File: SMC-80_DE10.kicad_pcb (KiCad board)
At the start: 4 copper layers, 63.5 x 58.4 mm, 26 parts, among them J1 Arduino1, J2 DE10-Lite GPIO, J3 Arduino2, J4 Port A, U1 SST39SF040, U2 Z84C0010AEG, U3 AS6C4008A-55ZIN, U4 Z84C4310AEG

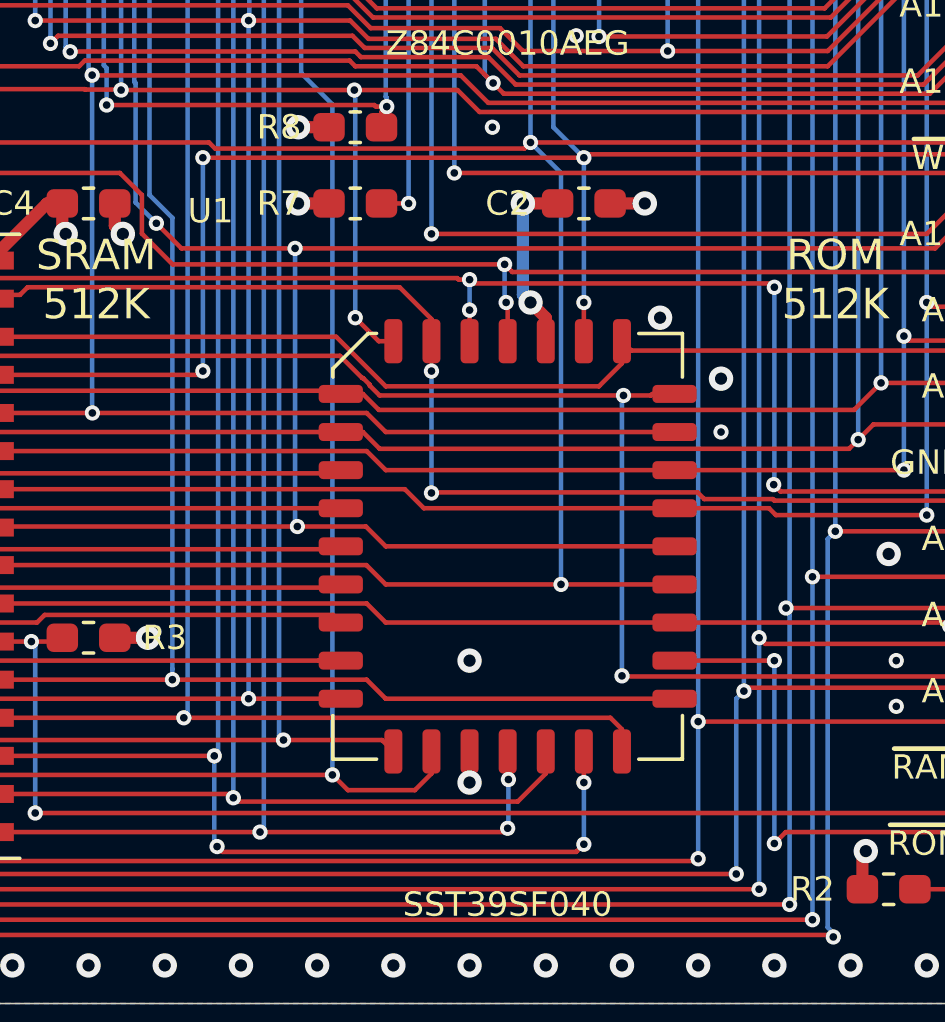
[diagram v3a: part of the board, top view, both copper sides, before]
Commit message: enhanced graphic for PLCC socket
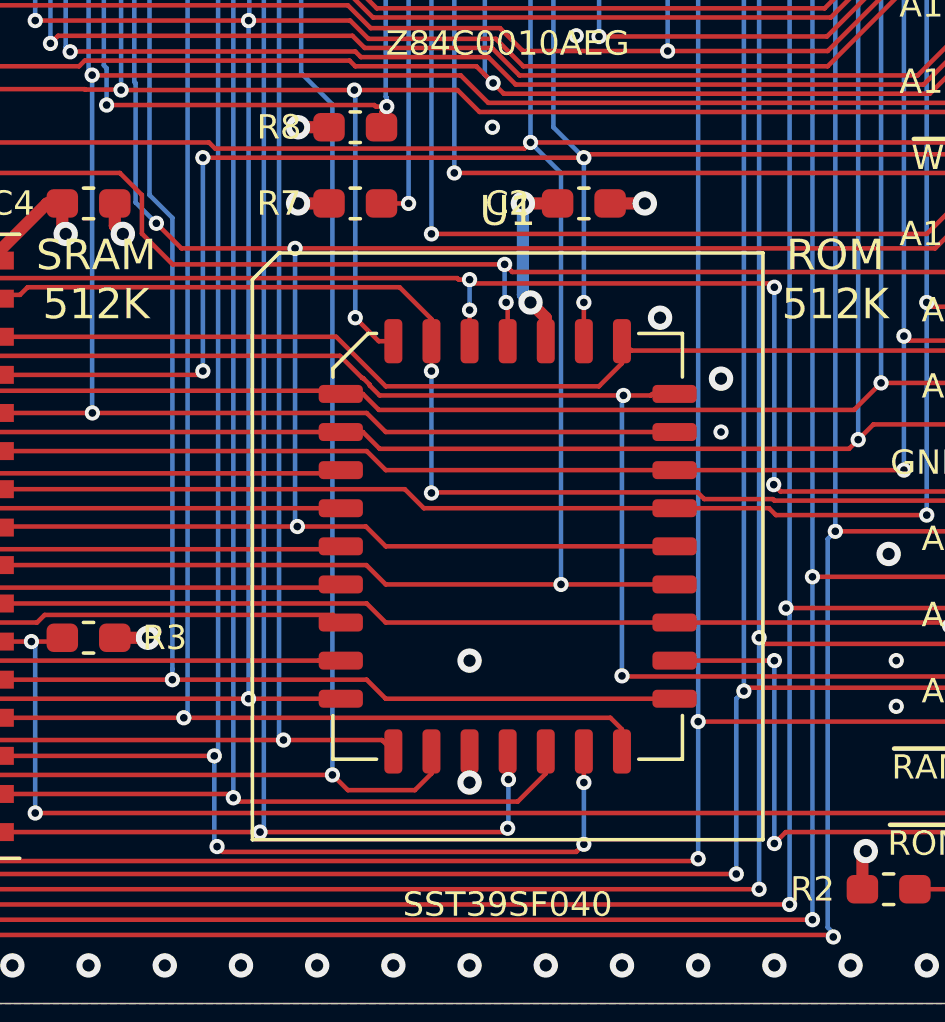
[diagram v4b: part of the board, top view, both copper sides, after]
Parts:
- U1: value SST39SF040 -> SST39LF040
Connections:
- J1 pad 1: (no net) -> Net-(J1-Pad1)
- J1 pad 2: (no net) -> Net-(J1-Pad2)
- J2 pad 1: (no net) -> Net-(J2-Pad1)
- J2 pad 11: (no net) -> +5V
- J2 pad 3: (no net) -> Net-(J2-Pad3)
- J2 pad 35: (no net) -> Net-(J2-Pad35)
- J2 pad 37: (no net) -> Net-(J2-Pad37)
- J3 pad 4: (no net) -> Net-(J3-Pad4)
- J3 pad 5: (no net) -> Net-(J3-Pad5)
- J3 pad 6: (no net) -> Net-(J3-Pad6)
- J3 pad 7: (no net) -> Net-(J3-Pad7)
- J3 pad 8: (no net) -> Net-(J3-Pad8)
- J4 pad 3: (no net) -> Net-(J4-Pad3)
- R2 pad 1: VCC -> Net-(R2-Pad1)
- U2 pad 11: (no net) -> Net-(U2-Pad11)
- U2 pad 17: (no net) -> Net-(U2-Pad17)
- U2 pad 20: (no net) -> Net-(U2-Pad20)
- U2 pad 25: (no net) -> Net-(U2-Pad25)
- U2 pad 33: (no net) -> Net-(U2-Pad33)
- U2 pad 39: (no net) -> Net-(U2-Pad39)
- U4 pad 1: (no net) -> Net-(U4-Pad1)
- U4 pad 10: (no net) -> Net-(U4-Pad10)
- U4 pad 11: (no net) -> Net-(U4-Pad11)
- U4 pad 12: (no net) -> Net-(U4-Pad12)
- U4 pad 13: (no net) -> Net-(U4-Pad13)
- U4 pad 14: (no net) -> Net-(U4-Pad14)
- U4 pad 15: (no net) -> Net-(U4-Pad15)
- U4 pad 16: (no net) -> Net-(U4-Pad16)
- U4 pad 17: (no net) -> Net-(U4-Pad17)
- U4 pad 28: (no net) -> Net-(U4-Pad28)
- U4 pad 35: (no net) -> Net-(U4-Pad35)
- U4 pad 38: (no net) -> Net-(U4-Pad38)
- U4 pad 39: (no net) -> Net-(U4-Pad39)
- U4 pad 40: (no net) -> Net-(U4-Pad40)
- U4 pad 8: (no net) -> Net-(U4-Pad8)
- U4 pad 9: (no net) -> Net-(U4-Pad9)
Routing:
- net Net-(R2-Pad1): track 0.00 -> 1.32 mm, vias 0 -> 1
- net VCC: track 32.2 -> 30.9 mm, vias 15 -> 14

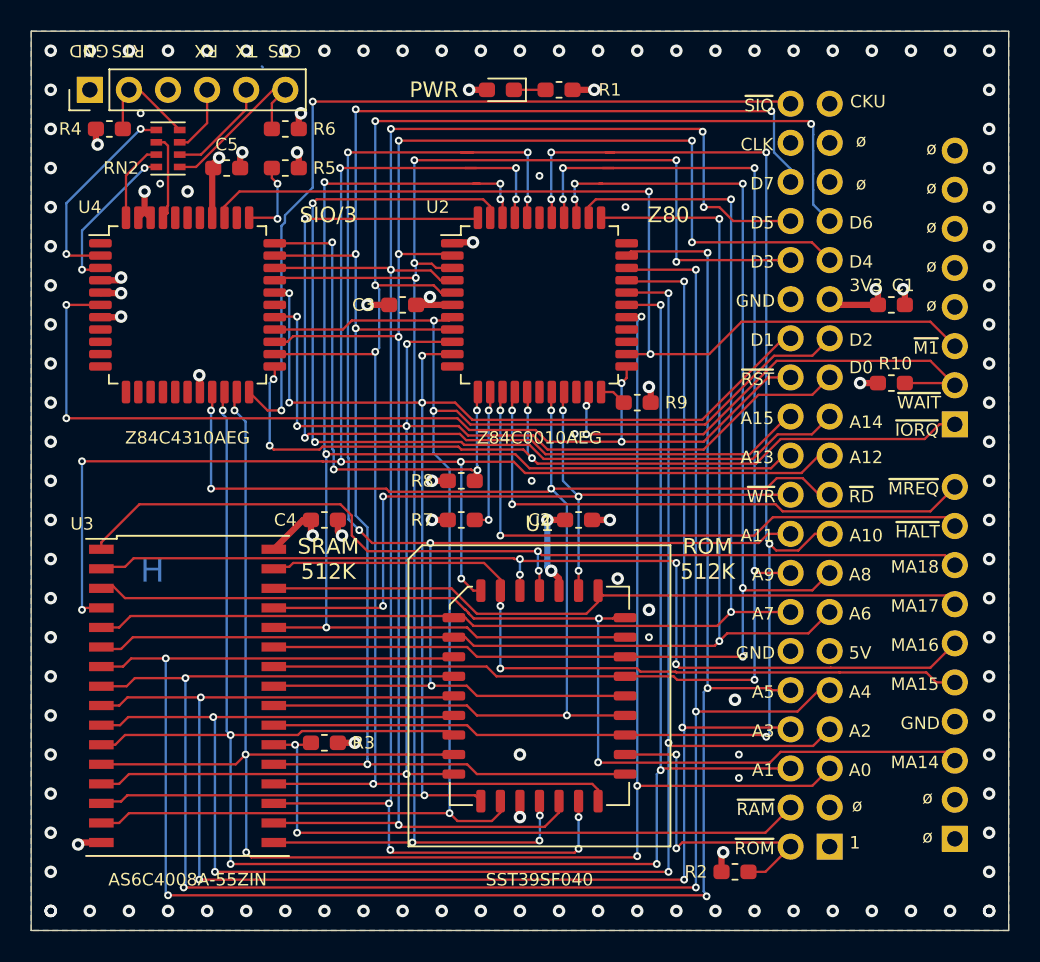
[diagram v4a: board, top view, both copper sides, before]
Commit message: removed ram/rom ce pullups
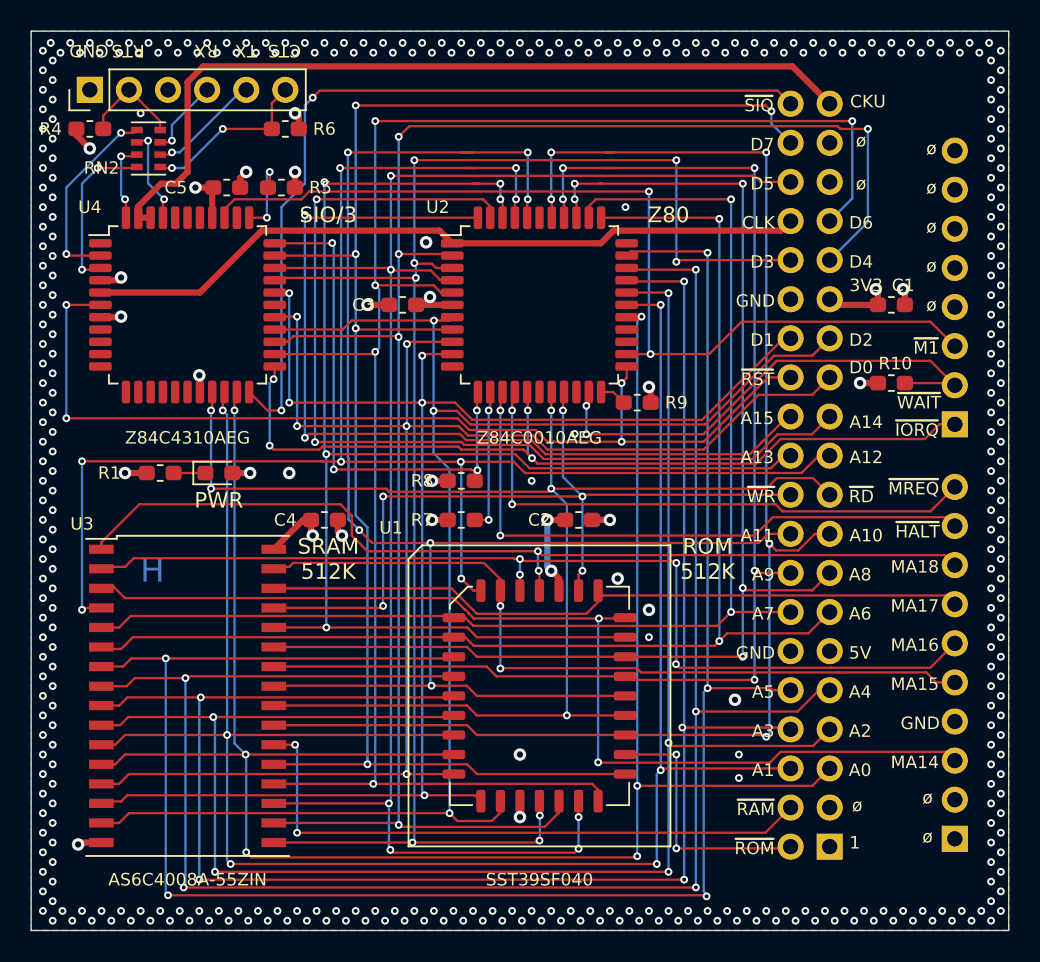
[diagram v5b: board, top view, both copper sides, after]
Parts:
- removed R2, R3: 10K, Resistor_SMD:R_0603_1608Metric_Pad1.05x0.95mm_HandSolder
- moved R1 35.9 mm to (108.7, 98.6), turned to 180 degrees
- moved D1 30.9 mm to (112.5, 98.6), turned to 0 degrees
- moved R5 1.30 mm to (116.6, 80.0)
- moved C5 1.27 mm to (113.0, 80.0)
- moved R4 1.27 mm to (104.1, 76.2)
- moved RN2 1.27 mm to (108.0, 77.5)
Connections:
- J2 pad 34: /D5 -> /CLK
- J2 pad 36: /D7 -> /D5
- J2 pad 38: /CLK -> /D7
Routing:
- net /D5: track 113.1 -> 104.9 mm, vias 8 -> 6
- net /D4: track 111.0 -> 116.6 mm, vias 6 -> 5
- net /CLK_U: track 49.9 -> 54.6 mm, vias 1 -> 0
- net /ROM_~CE: track 20.5 -> 16.9 mm
- net /CLK: track 50.9 -> 47.6 mm, vias 2 -> 0
- net /D6: track 112.3 -> 115.2 mm
- net /D7: track 109.7 -> 107.5 mm
- net VCC: track 30.9 -> 29.4 mm, vias 14 -> 13
- net Net-(R2-Pad1): track 1.32 -> 0.00 mm, vias 1 -> 0
- net Net-(J4-Pad4): track 4.46 -> 5.59 mm, vias 0 -> 1
- net /RAM_~CE: track 41.0 -> 39.9 mm
- net Net-(J4-Pad2): track 7.08 -> 7.93 mm
- net /SIO_~CE: track 54.8 -> 55.5 mm
- net /Ram Rom and CPU/~RTS: track 13.4 -> 12.8 mm
- net /Ram Rom and CPU/RX: track 5.66 -> 6.25 mm, vias 0 -> 2
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
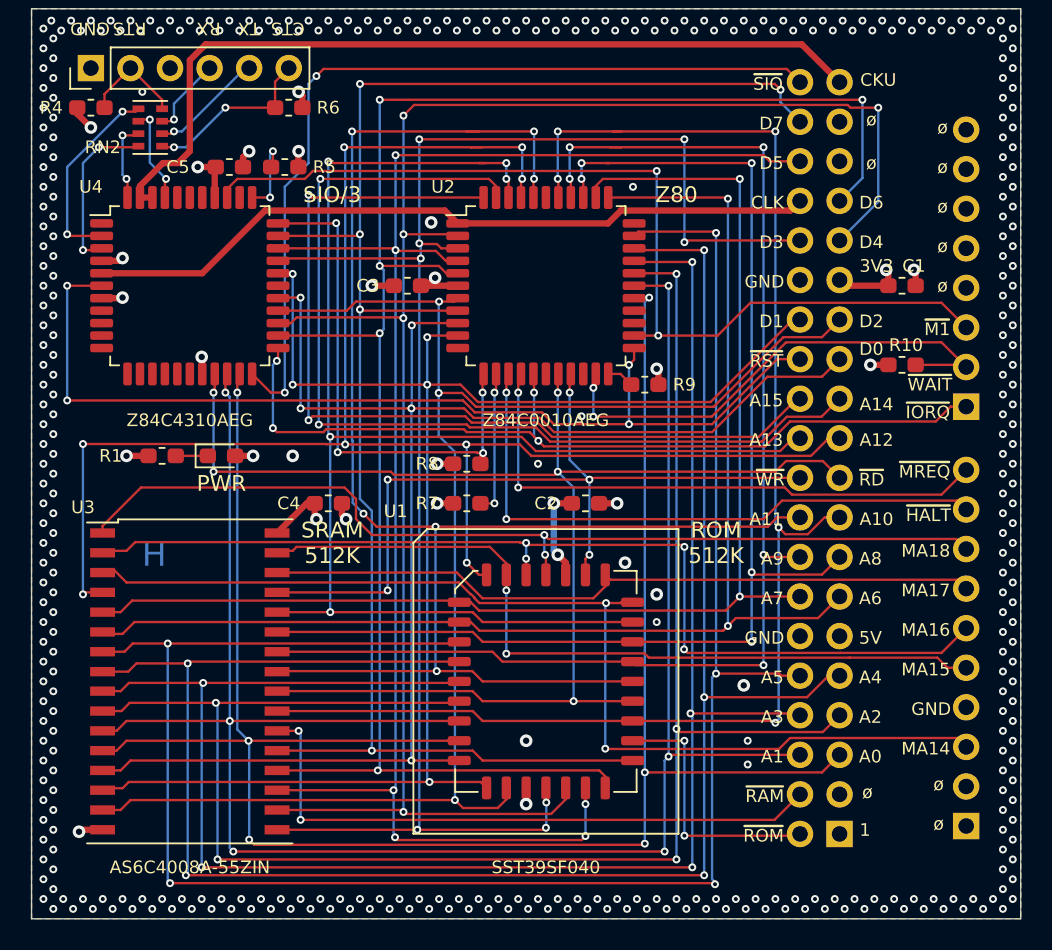
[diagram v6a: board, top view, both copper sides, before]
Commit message: shifted Arduino pins
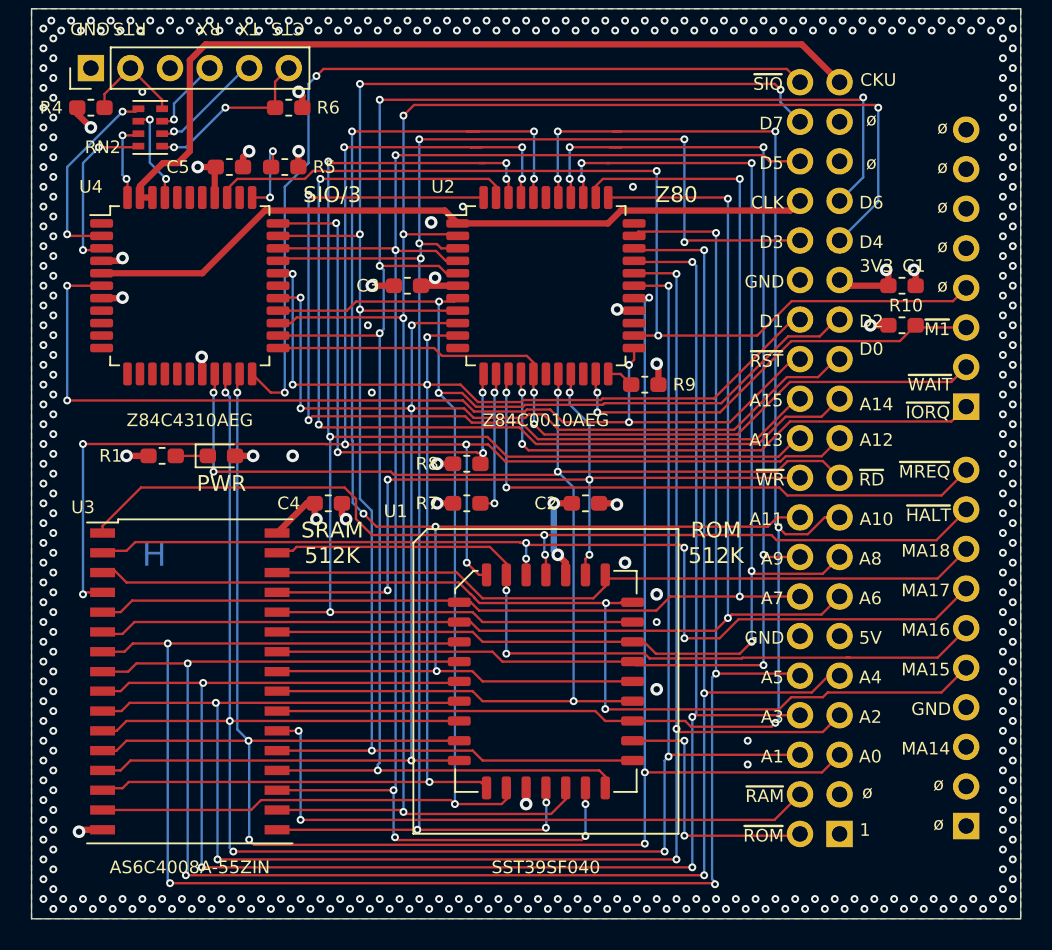
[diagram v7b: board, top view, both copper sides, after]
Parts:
- moved R10 2.54 mm to (156.2, 90.2)
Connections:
- J1 pad 10: /~MREQ -> /~HALT
- J1 pad 3: /MA14 -> Net-(J1-Pad3)
- J1 pad 5: /MA15 -> /MA14
- J1 pad 6: /MA16 -> /MA15
- J1 pad 7: /MA17 -> /MA16
- J1 pad 8: /MA18 -> /MA17
- J1 pad 9: /~HALT -> /MA18
- J3 pad 1: /~IORQ -> /~MREQ
- J3 pad 2: /~WAIT -> /~IORQ
- J3 pad 3: /~M1 -> /~WAIT
- J3 pad 4: Net-(J3-Pad4) -> /~M1
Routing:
- net /~IORQ: track 55.9 -> 50.6 mm, vias 4 -> 2
- net /~WAIT: track 32.7 -> 28.6 mm
- net /~MREQ: track 37.0 -> 34.6 mm
- net /MA14: track 68.1 -> 66.1 mm
- net /~HALT: track 39.6 -> 37.8 mm
- net GND: track 15.0 -> 16.2 mm, vias 397 -> 398
- net /MA15: track 51.0 -> 51.8 mm
- net /A8: track 81.0 -> 81.6 mm
- net /MA17: track 46.3 -> 46.9 mm
- net /A6: track 84.0 -> 83.5 mm

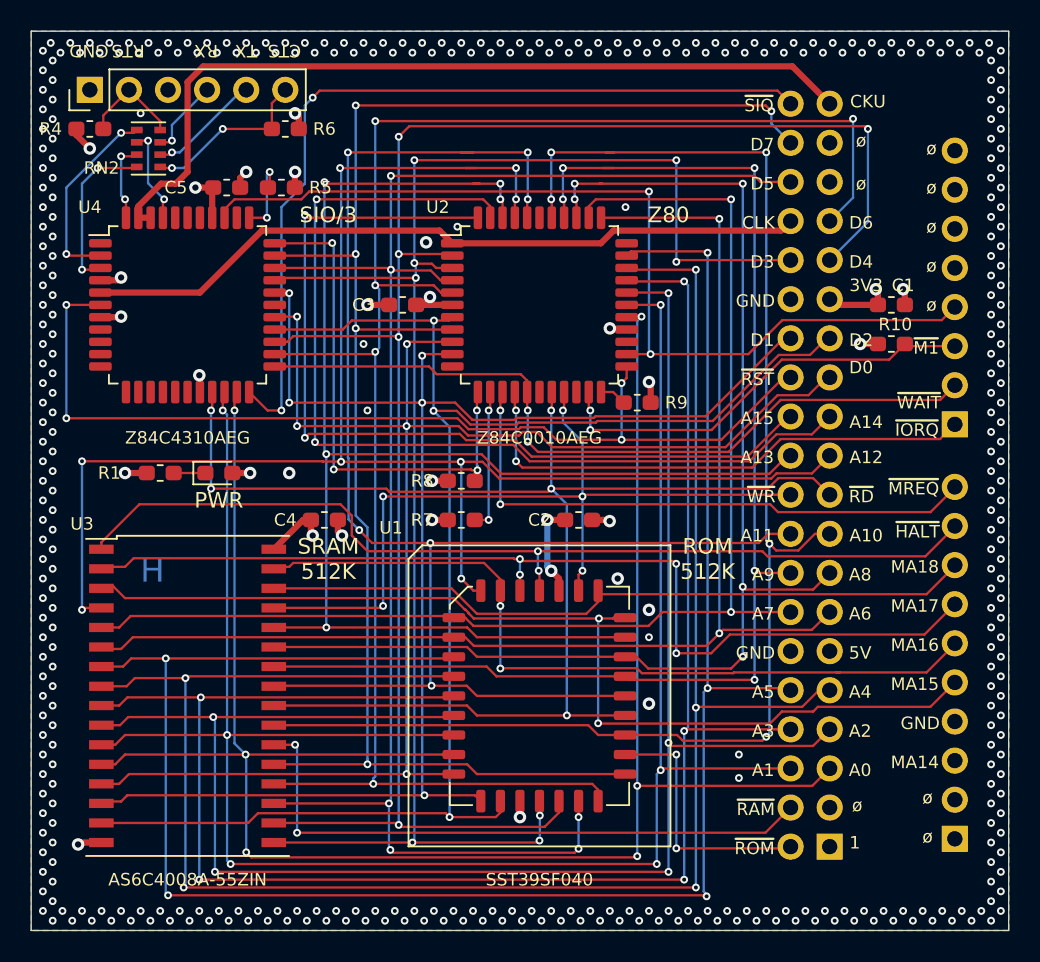
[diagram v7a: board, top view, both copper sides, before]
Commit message: shifted some components
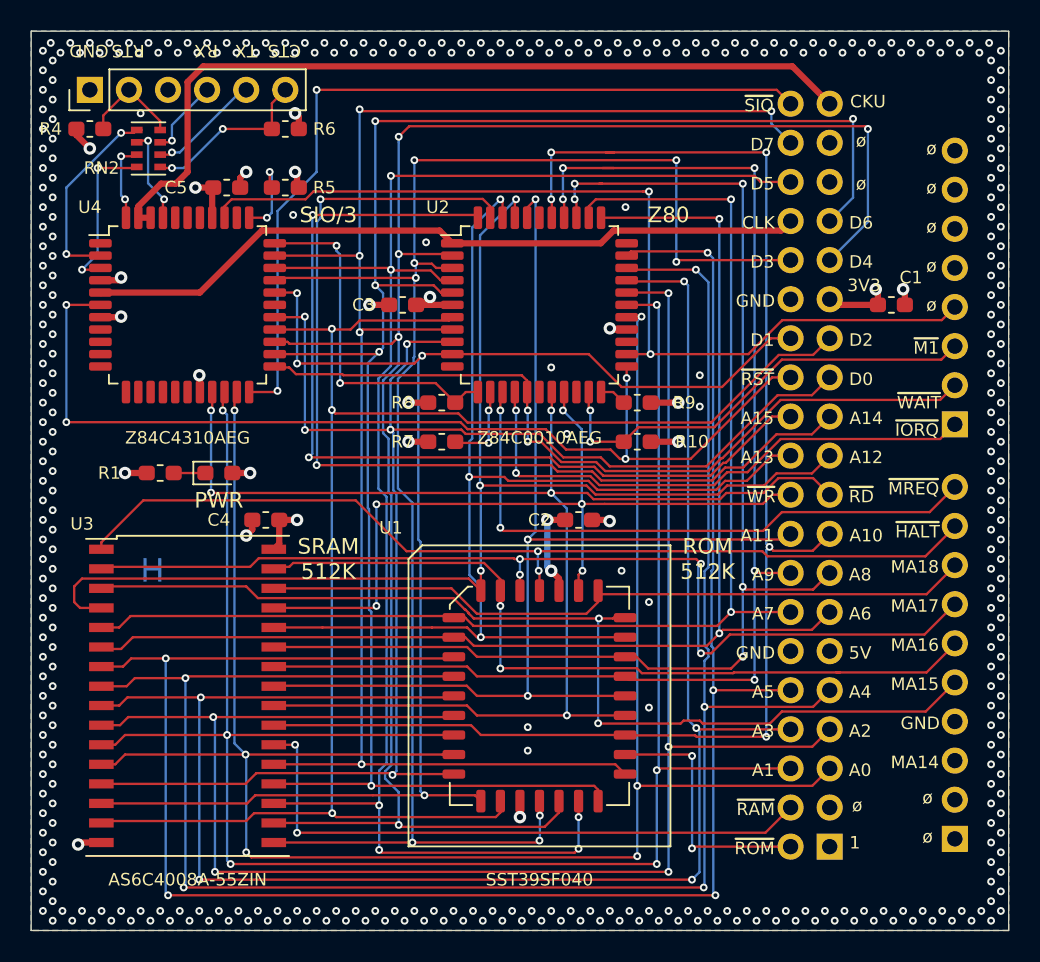
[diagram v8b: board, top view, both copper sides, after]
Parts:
- moved R10 17.7 mm to (139.7, 96.5), turned to 0 degrees
- moved R7 5.24 mm to (127.0, 96.5)
- moved R8 5.24 mm to (127.0, 94.0)
- moved C4 3.81 mm to (115.6, 101.6), turned to 180 degrees
- moved R5 0.25 mm to (116.8, 80.0)
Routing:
- net /A11: track 102.6 -> 74.2 mm, vias 6 -> 3
- net /A12: track 104.3 -> 81.5 mm, vias 8 -> 3
- net /A13: track 97.4 -> 76.1 mm, vias 5 -> 3
- net /Ram Rom and CPU/~INT: track 33.7 -> 23.0 mm, vias 4 -> 2
- net /D2: track 100.1 -> 105.4 mm
- net /D1: track 98.9 -> 94.4 mm, vias 5 -> 4
- net /Ram Rom and CPU/~NMI: track 9.25 -> 5.55 mm
- net /~RESET: track 63.9 -> 66.1 mm
- net /~HALT: track 37.8 -> 39.7 mm
- net /D0: track 99.9 -> 101.8 mm
- net /SIO_~CE: track 55.5 -> 53.8 mm
- net /A14: track 63.2 -> 64.8 mm
- net /~MREQ: track 34.6 -> 36.0 mm
- net /D4: track 116.6 -> 117.8 mm
- net /~IORQ: track 50.6 -> 51.6 mm
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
